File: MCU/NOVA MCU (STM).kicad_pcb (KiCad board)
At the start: 2 copper layers, 125 x 105 mm, 44 parts, among them J1101 Conn_01x06_Male, J501 Conn_01x12_Male, J502 Conn_01x12_Male, J503 Conn_01x12_Male, J504 Conn_01x12_Male, J601 USB_C_Receptacle, J801 Connector_Generic_Conn_01x02, U301 STM32F401RBTx, U601 FT234XD-R, U701 MIC5219-3_3YM5-TR, Y401 ECS-260-8-36B-CKY-TR, Y402 JTX310

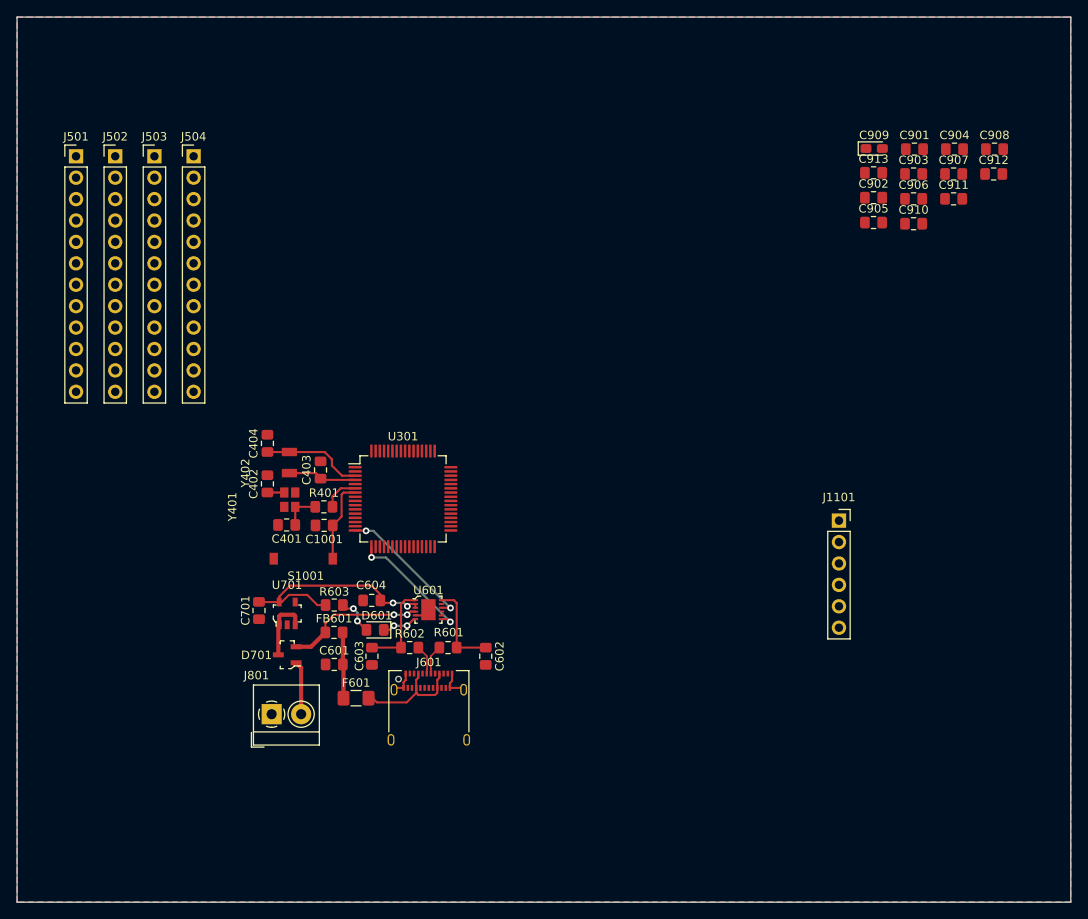
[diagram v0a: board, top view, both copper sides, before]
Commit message: Finalized Schematic. Finished PCB routing. Needs silkscreen
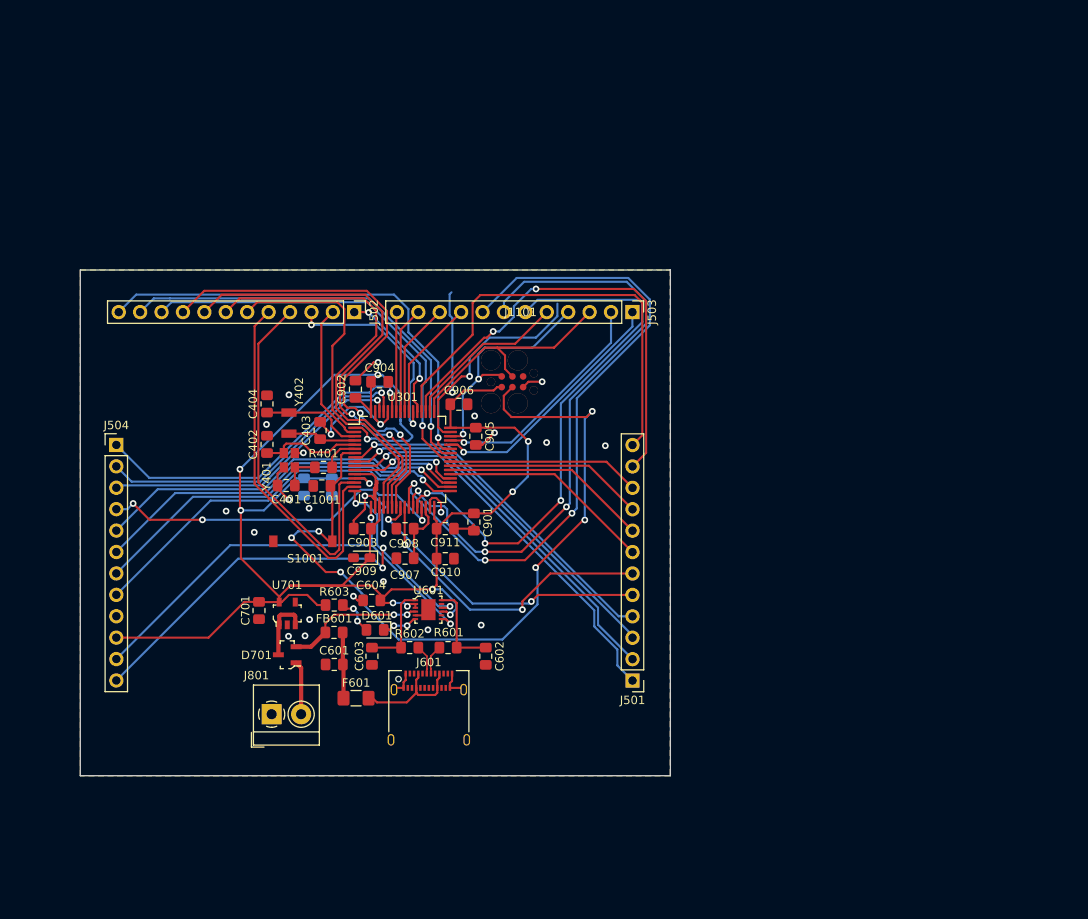
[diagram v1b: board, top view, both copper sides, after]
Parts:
- C912, C913: moved to B.Cu
- J1101: footprint Connector_PinSocket_2.54mm:PinSocket_1x06_P2.54mm_Vertical -> Red:j-link_6_pin_needle
- moved J501 90.7 mm to (158.0, 123.7), turned to 180 degrees
- moved C912 89.8 mm to (119.0, 100.7), turned to 270 degrees
- moved C908 83.2 mm to (131.0, 105.7)
- moved C907 79.5 mm to (131.0, 109.2)
- moved C909 77.8 mm to (125.9, 109.1), turned to 180 degrees
- moved C903 77.8 mm to (126.0, 105.7), turned to 180 degrees
- moved C913 74.3 mm to (122.3, 100.8), turned to 270 degrees
- moved C904 73.6 mm to (128.0, 88.3)
- moved C911 71.9 mm to (135.8, 105.7)
- moved C901 68.5 mm to (139.2, 104.9), turned to 270 degrees
- moved C910 68.3 mm to (135.8, 109.2)
- moved C902 65.5 mm to (125.1, 89.2), turned to 90 degrees
- moved J503 59.6 mm to (158.0, 80.0), turned to 270 degrees
- moved C906 59.2 mm to (137.4, 90.9)
- moved C905 53.6 mm to (139.4, 94.7), turned to 270 degrees
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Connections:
- J1101 pad 3: /STM32F401RBT6/Pin Headers/27 -> /STM32F401RBT6/MCU/RESET
- J1101 pad 4: /STM32F401RBT6/MCU/RESET -> /STM32F401RBT6/Pin Headers/27
- J501 pad 1: /STM32F401RBT6/Pin Headers/1 -> /STM32F401RBT6/Pin Headers/4
- J501 pad 2: /STM32F401RBT6/Pin Headers/2 -> /STM32F401RBT6/Pin Headers/3
- J501 pad 3: /STM32F401RBT6/Pin Headers/3 -> /STM32F401RBT6/Pin Headers/2
- J501 pad 4: /STM32F401RBT6/Pin Headers/4 -> /STM32F401RBT6/Pin Headers/1
- J503 pad 6: /STM32F401RBT6/Pin Headers/30 -> /STM32F401RBT6/Pin Headers/32
- J503 pad 8: /STM32F401RBT6/Pin Headers/32 -> /STM32F401RBT6/Pin Headers/30
- J504 pad 5: /STM32F401RBT6/Pin Headers/41 -> /STM32F401RBT6/Pin Headers/44
- J504 pad 6: /STM32F401RBT6/Pin Headers/42 -> /STM32F401RBT6/Pin Headers/43
- J504 pad 7: /STM32F401RBT6/Pin Headers/43 -> /STM32F401RBT6/Pin Headers/42
- J504 pad 8: /STM32F401RBT6/Pin Headers/44 -> /STM32F401RBT6/Pin Headers/41
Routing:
- net +3V3: track 28.1 -> 208.6 mm, vias 2 -> 11
- net GND: track 8.37 -> 105.4 mm, vias 0 -> 27
- net /STM32F401RBT6/MCU/RESET: track 9.75 -> 94.8 mm, vias 0 -> 6
- net /STM32F401RBT6/Pin Headers/30: track 0.00 -> 80.8 mm, vias 0 -> 3
- net /STM32F401RBT6/Pin Headers/31: track 0.00 -> 74.5 mm, vias 0 -> 3
- net /STM32F401RBT6/Pin Headers/32: track 0.00 -> 65.1 mm, vias 0 -> 3
- net /STM32F401RBT6/Pin Headers/21: track 0.00 -> 57.9 mm, vias 0 -> 2
- net /STM32F401RBT6/Pin Headers/24: track 0.00 -> 55.1 mm, vias 0 -> 1
- net /STM32F401RBT6/Pin Headers/11: track 0.00 -> 54.9 mm, vias 0 -> 2
- net /STM32F401RBT6/Pin Headers/12: track 0.00 -> 53.7 mm
- net /STM32F401RBT6/Pin Headers/20: track 0.00 -> 53.6 mm, vias 0 -> 2
- net /STM32F401RBT6/Pin Headers/23: track 0.00 -> 50.7 mm, vias 0 -> 1
- net /STM32F401RBT6/Pin Headers/19: track 0.00 -> 49.6 mm
- net /STM32F401RBT6/Pin Headers/22: track 0.00 -> 48.4 mm, vias 0 -> 1
- net /STM32F401RBT6/Pin Headers/41: track 0.00 -> 47.9 mm, vias 0 -> 1
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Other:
- board size 125 x 105 mm -> 70 x 60 mm

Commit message: Finished Schematic and pcb. Ready for review.
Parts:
- removed D701: BAT54C-7-F, digikey-footprints:SOT-23-3
- removed J801: Connector_Generic_Conn_01x02, TerminalBlock_4Ucon:TerminalBlock_4Ucon_1x02_P3.50mm_Horizontal
- added R604: 5K, Resistor_SMD:R_0805_2012Metric_Pad1.15x1.40mm_HandSolder, F.Cu at (141.5, 127.7)
- added R605: 5K, Resistor_SMD:R_0805_2012Metric_Pad1.15x1.40mm_HandSolder, F.Cu at (141.5, 124.0)
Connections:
- U701 pad 1: Net-(D701-Pad3) -> /STM32F401RBT6/REGULATOR /VUSB
- U701 pad 3: Net-(D701-Pad3) -> /STM32F401RBT6/REGULATOR /VUSB
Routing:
- net Net-(J601-PadA5): track 0.00 -> 10.2 mm, vias 0 -> 2
- net Net-(J601-PadB5): track 0.00 -> 8.39 mm, vias 0 -> 2
- net /STM32F401RBT6/REGULATOR /VUSB: track 16.5 -> 24.7 mm
- net Net-(D701-Pad3): track 7.69 -> 0.00 mm
- net /STM32F401RBT6/BATTERY/BATTERY: track 6.35 -> 0.00 mm
- net Net-(F601-Pad2): track 13.9 -> 17.1 mm
- net GND: track 105.4 -> 106.5 mm, vias 27 -> 25
- net +3V3: track 208.6 -> 207.7 mm
- net /STM32F401RBT6/Pin Headers/41: track 47.9 -> 47.1 mm
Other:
- board text added: "+3V3"
- board text added: "GND"
- board text added: "PA0"
- board text added: "PA1"
- board text added: "PA10"
- board text added: "PA11"
- board text added: "PA12"
- board text added: "PA13"
- board text added: "PA14"
- board text added: "PA15"
- board text added: "PA4"
- board text added: "PA5"
- board text added: "PA6"
- board text added: "PA7"
- board text added: "PA8"
- board text added: "PA9"
- board text added: "PB0"
- board text added: "PB1"
- board text added: "PB10"
- board text added: "PB12"
- board text added: "PB13"
- board text added: "PB14"
- board text added: "PB15"
- board text added: "PB2"
- board text added: "PB3"
- board text added: "PB4"
- board text added: "PB5"
- board text added: "PB6"
- board text added: "PB7"
- board text added: "PB8"
- board text added: "PB9"
- board text added: "PC0"
- board text added: "PC1"
- board text added: "PC10"
- board text added: "PC11"
- board text added: "PC12"
- board text added: "PC13"
- board text added: "PC2"
- board text added: "PC3"
- board text added: "PC4"
- board text added: "PC5"
- board text added: "PC6"
- board text added: "PC7"
- board text added: "PC8"
- board text added: "PC9"
- board text added: "PD2"
- board text added: "RXD"
- board text added: "TXD"

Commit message: Final board design for review
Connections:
- net /STM32F401RBT6/Pin Headers/27 renamed /STM32F401RBT6/SWCLK
- net /STM32F401RBT6/Pin Headers/28 renamed /STM32F401RBT6/SWDIO
- net /STM32F401RBT6/Pin Headers/47 renamed /STM32F401RBT6/RXD
- net /STM32F401RBT6/Pin Headers/48 renamed /STM32F401RBT6/TXD
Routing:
- net GND: track 106.5 -> 107.0 mm, vias 25 -> 26

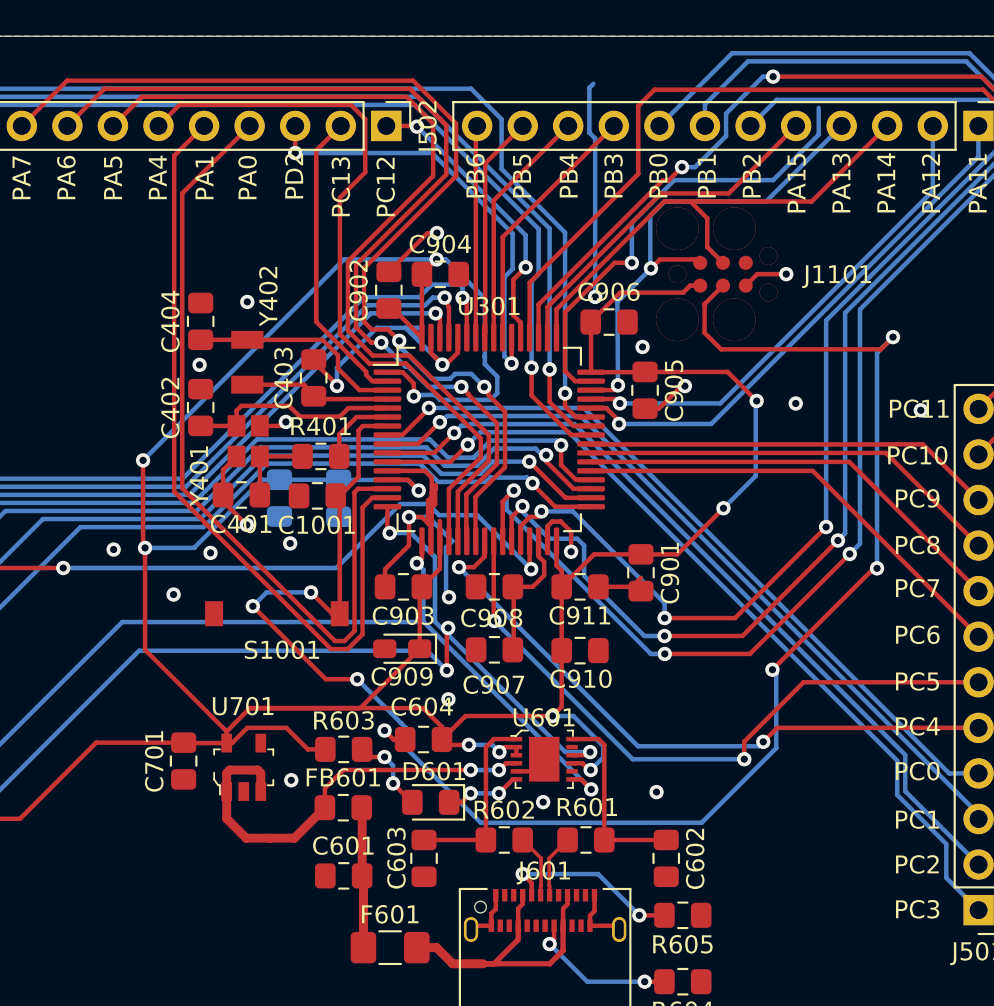
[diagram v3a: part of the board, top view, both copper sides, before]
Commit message: Added Footprint and Symbol Libraries
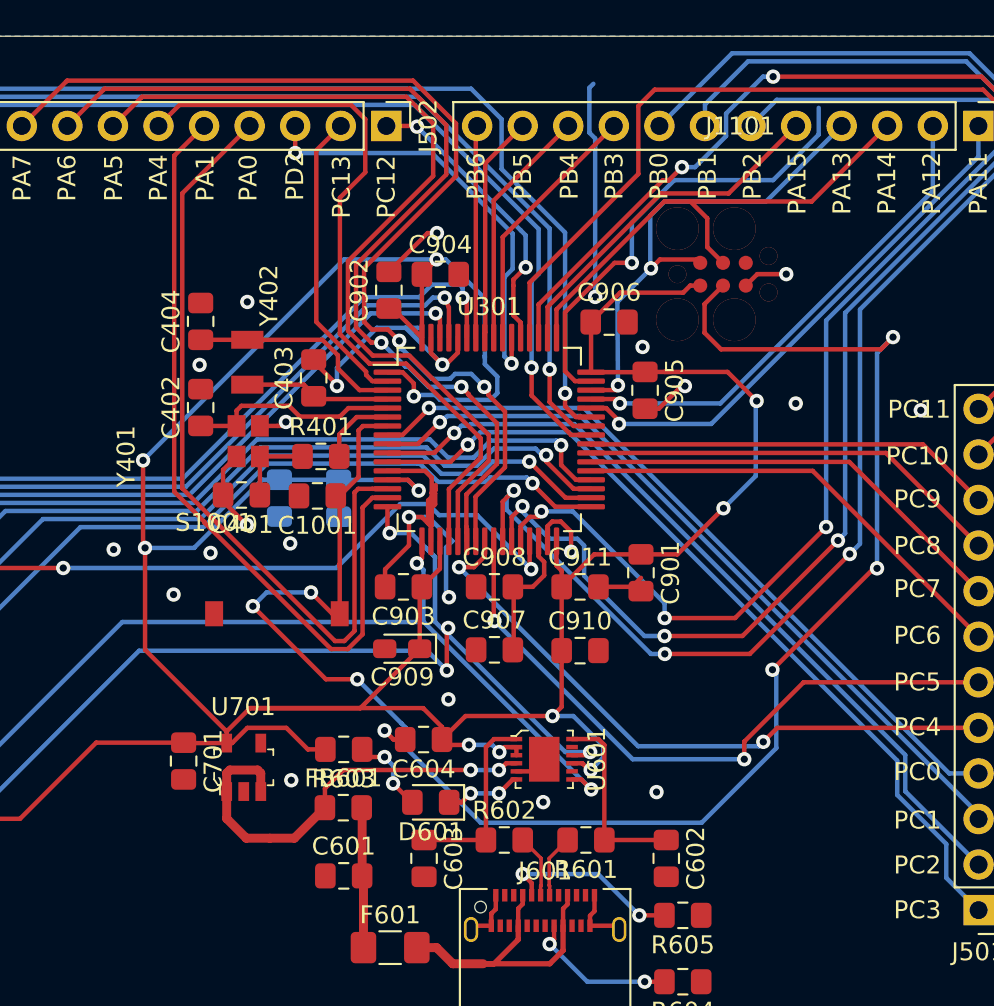
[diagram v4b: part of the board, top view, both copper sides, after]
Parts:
- C1001, C401, C402, C403, C404, C601, C602, C603, C604, C701, C901, C902, C903, C904, C905, C906, C907, C908, C910, C911, C912, C913: footprint Capacitor_SMD:C_0805_2012Metric_Pad1.15x1.40mm_HandSolder -> NOVA MCU (STM):C_0805_2012Metric_Pad1.15x1.40mm_HandSolder
- C909: footprint Capacitor_Tantalum_SMD:CP_EIA-2012-15_AVX-P_Pad1.30x1.05mm_HandSolder -> NOVA MCU (STM):CP_EIA-2012-15_AVX-P_Pad1.30x1.05mm_HandSolder
- D601: footprint LED_SMD:LED_0805_2012Metric_Pad1.15x1.40mm_HandSolder -> NOVA MCU (STM):LED_0805_2012Metric_Pad1.15x1.40mm_HandSolder
- F601: footprint Fuse:Fuse_1206_3216Metric_Pad1.42x1.75mm_HandSolder -> NOVA MCU (STM):Fuse_1206_3216Metric_Pad1.42x1.75mm_HandSolder
- FB601, R401, R601, R602, R603, R604, R605: footprint Resistor_SMD:R_0805_2012Metric_Pad1.15x1.40mm_HandSolder -> NOVA MCU (STM):R_0805_2012Metric_Pad1.15x1.40mm_HandSolder
- J1101: footprint Red:j-link_6_pin_needle -> NOVA MCU (STM):j-link_6_pin_needle
- J501, J502, J503, J504: footprint Connector_PinHeader_2.54mm:PinHeader_1x12_P2.54mm_Vertical -> NOVA MCU (STM):PinHeader_1x12_P2.54mm_Vertical
- J601: footprint Connector_USB:USB_C_Receptacle_Amphenol_12401610E4-2A -> NOVA MCU (STM):USB_C_Receptacle_Amphenol_12401610E4-2A
- S1001: footprint NOVA FOOTPRINTS:KSR223GLFG -> NOVA MCU (STM):KSR223GLFG
- U301: footprint Package_QFP:LQFP-64_10x10mm_P0.5mm -> NOVA MCU (STM):LQFP-64_10x10mm_P0.5mm
- U601: footprint digikey-footprints:DFN-12-1EP_3x3mm -> NOVA MCU (STM):DFN-12-1EP_3x3mm
- U701: footprint digikey-footprints:SOT-753 -> NOVA MCU (STM):SOT-753
- Y401: footprint NOVA FOOTPRINTS:ECX-2236B -> NOVA MCU (STM):ECX-2236B
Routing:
- net +3V3: track 207.7 -> 206.5 mm
